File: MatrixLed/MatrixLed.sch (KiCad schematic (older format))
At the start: 68 parts

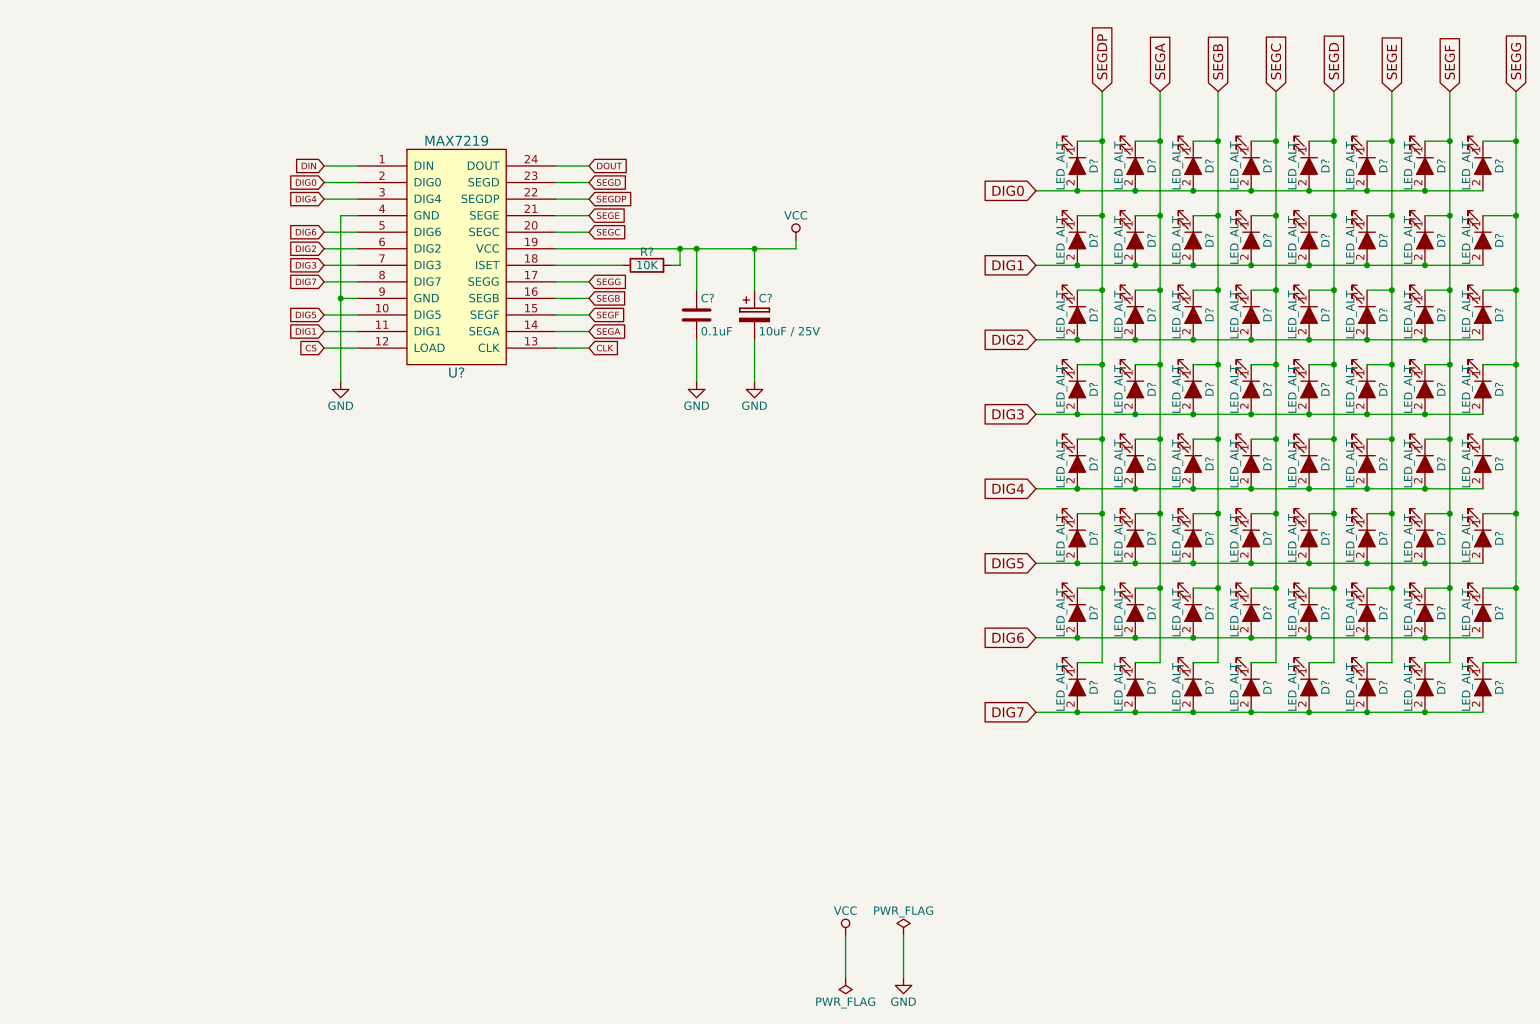
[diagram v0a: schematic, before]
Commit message: Leds girados para cambiar el MAX7219 por el HT16K33
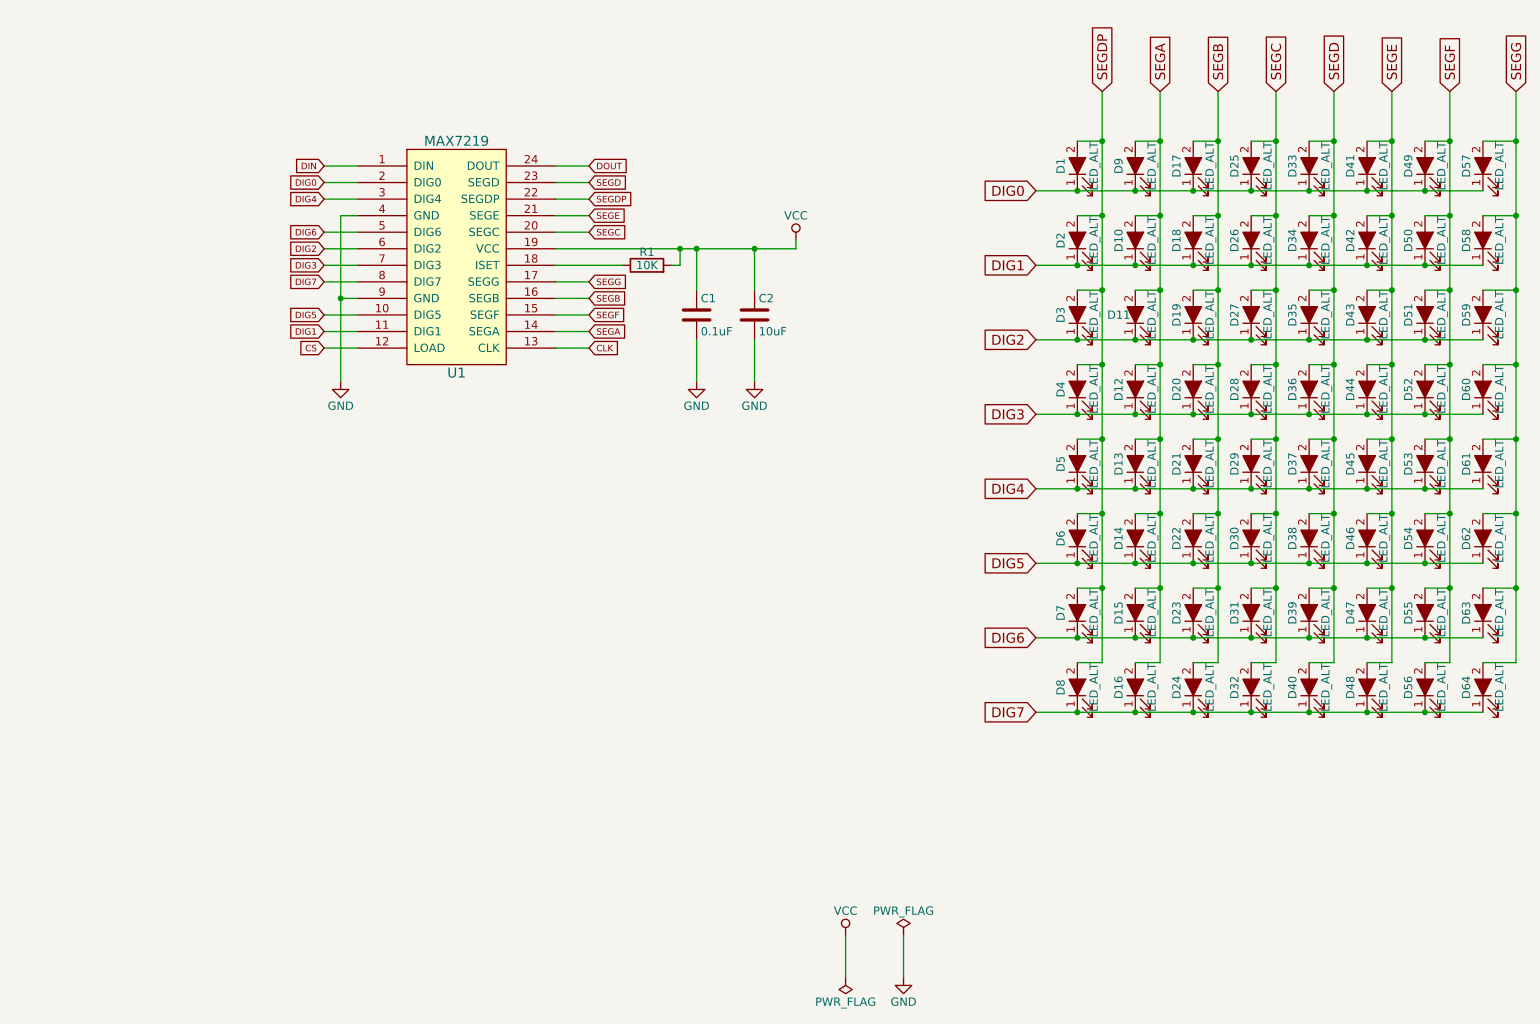
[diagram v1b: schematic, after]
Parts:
- removed C?: 10uF / 25V, symbol CP
- added C2: 10uF, symbol C
- gave numbers to parts that had none: 67
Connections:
- net DIG0: now also D1.1 (K), D17.1 (K), D25.1 (K), D33.1 (K), D41.1 (K), D49.1 (K), D57.1 (K), D9.1 (K); no longer D1.2 (A), D17.2 (A), D25.2 (A), D33.2 (A), D41.2 (A), D49.2 (A), D57.2 (A), D9.2 (A)
- net DIG1: now also D10.1 (K), D18.1 (K), D2.1 (K), D26.1 (K), D34.1 (K), D42.1 (K), D50.1 (K), D58.1 (K); no longer D10.2 (A), D18.2 (A), D2.2 (A), D26.2 (A), D34.2 (A), D42.2 (A), D50.2 (A), D58.2 (A)
- net DIG2: now also D11.1 (K), D19.1 (K), D27.1 (K), D3.1 (K), D35.1 (K), D43.1 (K), D51.1 (K), D59.1 (K); no longer D11.2 (A), D19.2 (A), D27.2 (A), D3.2 (A), D35.2 (A), D43.2 (A), D51.2 (A), D59.2 (A)
- net DIG3: now also D12.1 (K), D20.1 (K), D28.1 (K), D36.1 (K), D4.1 (K), D44.1 (K), D52.1 (K), D60.1 (K); no longer D12.2 (A), D20.2 (A), D28.2 (A), D36.2 (A), D4.2 (A), D44.2 (A), D52.2 (A), D60.2 (A)
- net DIG4: now also D13.1 (K), D21.1 (K), D29.1 (K), D37.1 (K), D45.1 (K), D5.1 (K), D53.1 (K), D61.1 (K); no longer D13.2 (A), D21.2 (A), D29.2 (A), D37.2 (A), D45.2 (A), D5.2 (A), D53.2 (A), D61.2 (A)
- net DIG5: now also D14.1 (K), D22.1 (K), D30.1 (K), D38.1 (K), D46.1 (K), D54.1 (K), D6.1 (K), D62.1 (K); no longer D14.2 (A), D22.2 (A), D30.2 (A), D38.2 (A), D46.2 (A), D54.2 (A), D6.2 (A), D62.2 (A)
- net DIG6: now also D15.1 (K), D23.1 (K), D31.1 (K), D39.1 (K), D47.1 (K), D55.1 (K), D63.1 (K), D7.1 (K); no longer D15.2 (A), D23.2 (A), D31.2 (A), D39.2 (A), D47.2 (A), D55.2 (A), D63.2 (A), D7.2 (A)
- net DIG7: now also D16.1 (K), D24.1 (K), D32.1 (K), D40.1 (K), D48.1 (K), D56.1 (K), D64.1 (K), D8.1 (K); no longer D16.2 (A), D24.2 (A), D32.2 (A), D40.2 (A), D48.2 (A), D56.2 (A), D64.2 (A), D8.2 (A)
- net GND: now also C2.2
- net SEGA: now also D10.2 (A), D11.2 (A), D12.2 (A), D13.2 (A), D14.2 (A), D15.2 (A), D16.2 (A), D9.2 (A); no longer D10.1 (K), D11.1 (K), D12.1 (K), D13.1 (K), D14.1 (K), D15.1 (K), D16.1 (K), D9.1 (K)
- net SEGB: now also D17.2 (A), D18.2 (A), D19.2 (A), D20.2 (A), D21.2 (A), D22.2 (A), D23.2 (A), D24.2 (A); no longer D17.1 (K), D18.1 (K), D19.1 (K), D20.1 (K), D21.1 (K), D22.1 (K), D23.1 (K), D24.1 (K)
- net SEGC: now also D25.2 (A), D26.2 (A), D27.2 (A), D28.2 (A), D29.2 (A), D30.2 (A), D31.2 (A), D32.2 (A); no longer D25.1 (K), D26.1 (K), D27.1 (K), D28.1 (K), D29.1 (K), D30.1 (K), D31.1 (K), D32.1 (K)
- net SEGD: now also D33.2 (A), D34.2 (A), D35.2 (A), D36.2 (A), D37.2 (A), D38.2 (A), D39.2 (A), D40.2 (A); no longer D33.1 (K), D34.1 (K), D35.1 (K), D36.1 (K), D37.1 (K), D38.1 (K), D39.1 (K), D40.1 (K)
- net SEGDP: now also D1.2 (A), D2.2 (A), D3.2 (A), D4.2 (A), D5.2 (A), D6.2 (A), D7.2 (A), D8.2 (A); no longer D1.1 (K), D2.1 (K), D3.1 (K), D4.1 (K), D5.1 (K), D6.1 (K), D7.1 (K), D8.1 (K)
- net SEGE: now also D41.2 (A), D42.2 (A), D43.2 (A), D44.2 (A), D45.2 (A), D46.2 (A), D47.2 (A), D48.2 (A); no longer D41.1 (K), D42.1 (K), D43.1 (K), D44.1 (K), D45.1 (K), D46.1 (K), D47.1 (K), D48.1 (K)
- net SEGF: now also D49.2 (A), D50.2 (A), D51.2 (A), D52.2 (A), D53.2 (A), D54.2 (A), D55.2 (A), D56.2 (A); no longer D49.1 (K), D50.1 (K), D51.1 (K), D52.1 (K), D53.1 (K), D54.1 (K), D55.1 (K), D56.1 (K)
- net SEGG: now also D57.2 (A), D58.2 (A), D59.2 (A), D60.2 (A), D61.2 (A), D62.2 (A), D63.2 (A), D64.2 (A); no longer D57.1 (K), D58.1 (K), D59.1 (K), D60.1 (K), D61.1 (K), D62.1 (K), D63.1 (K), D64.1 (K)
- net VCC: now also C2.1
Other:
- moved on the sheet: D1, D10, D11, D12, D13, D14, D15, D16, D17, D18, D19, D2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

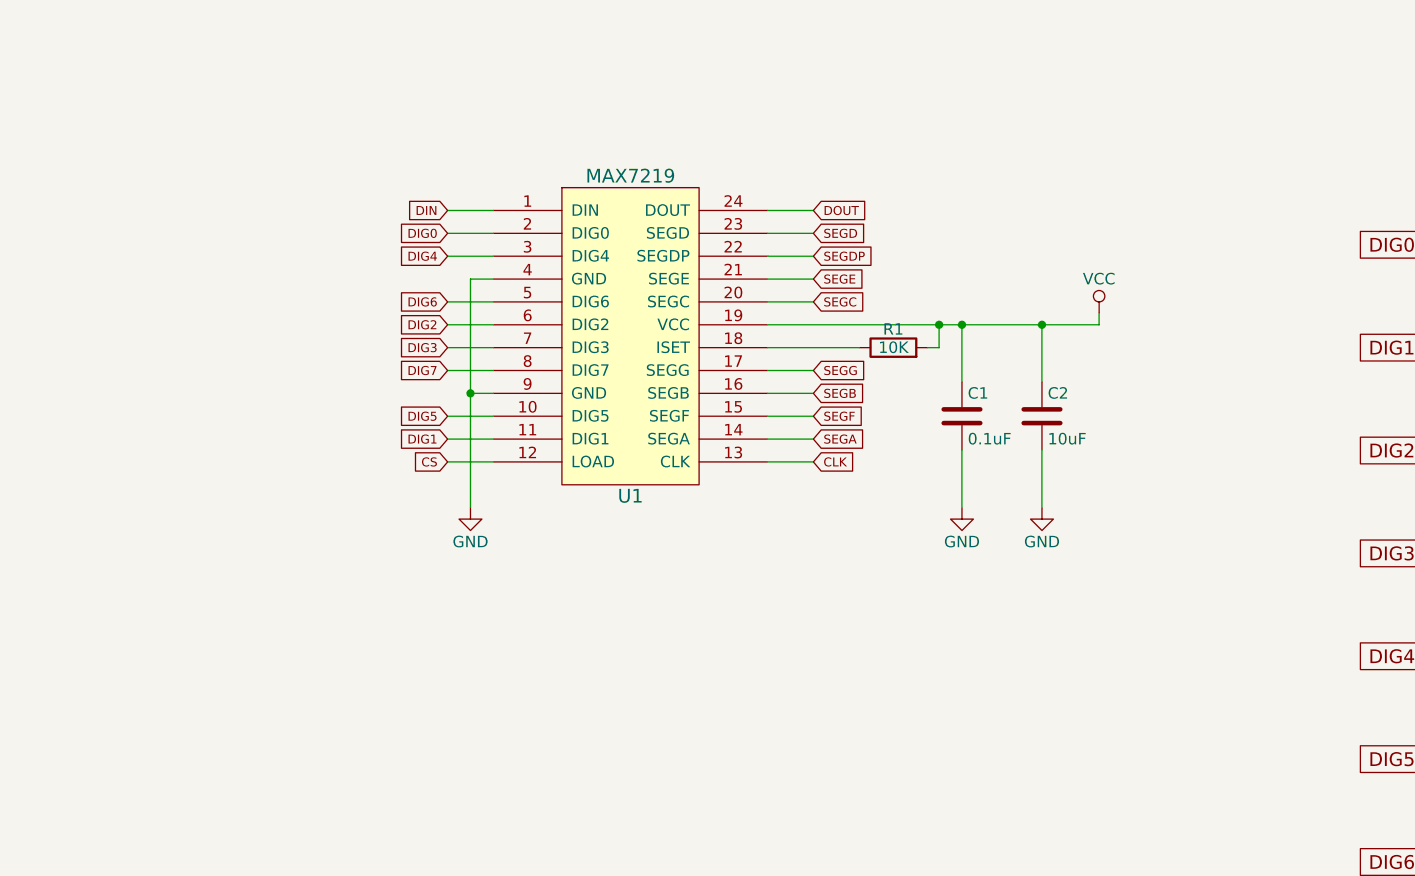
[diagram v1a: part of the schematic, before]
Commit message: Esquema terminado con el HT16K33, anotaciones hechas
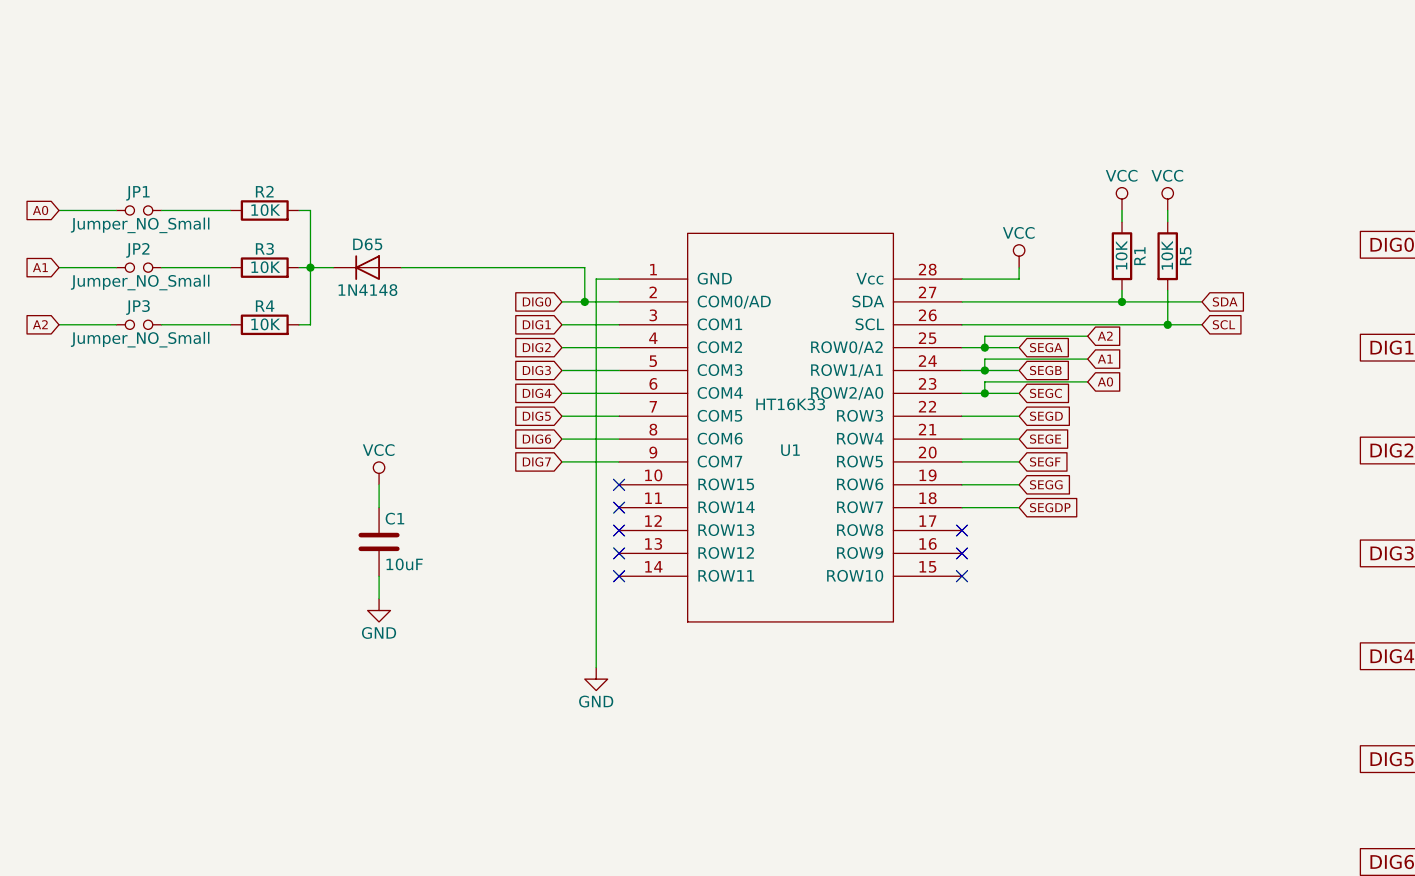
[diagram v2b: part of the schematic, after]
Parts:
- removed C2: 10uF, symbol C
- removed U1: MAX7219, symbol MAX7219
- added D65: 1N4148, Diodes_ThroughHole:D_DO-35_SOD27_Horizontal_RM10, symbol 1N4148
- added JP1, JP2, JP3: Jumper_NO_Small, symbol Jumper_NO_Small
- added R2, R3, R4, R5: 10K, symbol R
- added U1: HT16K33, MODULE, symbol HT16K33
- C1: value 0.1uF -> 10uF
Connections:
- net DIG0: now also D65.2 (A), U1.2 (COM0/AD)
- net DIG1: now also U1.3 (COM1)
- net DIG2: now also U1.4 (COM2)
- net DIG3: now also U1.5 (COM3)
- net DIG4: now also U1.6 (COM4)
- net DIG5: now also U1.7 (COM5)
- net DIG6: now also U1.8 (COM6)
- net DIG7: now also U1.9 (COM7)
- net GND: now also U1.1 (GND)
- net SEGD: now also U1.22 (ROW3)
- net SEGDP: now also U1.18 (ROW7)
- net SEGE: now also U1.21 (ROW4)
- net SEGF: now also U1.20 (ROW5)
- net SEGG: now also U1.19 (ROW6)
- net VCC: now also R1.1, R5.1, U1.28 (Vcc); no longer R1.2
- net SEGA renamed A2
- net A2: now also JP3.1, U1.25 (ROW0/A2)
- net SEGB renamed A1
- net A1: now also JP2.1, U1.24 (ROW1/A1)
- net SEGC renamed A0
- net A0: now also JP1.1, U1.23 (ROW2/A0)
- new net: JP1.2, R2.1
- new net: JP2.2, R3.1
- new net: JP3.2, R4.1
- new net: D65.1 (K), R2.2, R3.2, R4.2
- new net SCL: R5.2, U1.26 (SCL)
- new net SDA: R1.2, U1.27 (SDA)
- no-connect marks 0 -> 8
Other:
- moved on the sheet: R1

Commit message: DRC pasado y conector I2C añadido
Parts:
- added P1: CONN_01X04, symbol CONN_01X04
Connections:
- net GND: now also P1.1 (P1)
- net SCL: now also P1.3 (P3)
- net SDA: now also P1.4 (P4)
- net VCC: now also P1.2 (P2)
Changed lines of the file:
@@
 $EndComp
 $Comp
-L GND #PWR3
+L GND #PWR01
 U 1 1 58F84C6F
 P 3650 4450
-F 0 "#PWR3" H 3650 4200 50  0001 C CNN
+F 0 "#PWR01" H 3650 4200 50  0001 C CNN
 F 1 "GND" H 3650 4300 50  0000 C CNN
 F 2 "" H 3650 4450 50  0001 C CNN
@@
 $EndComp
 $Comp
-L VCC #PWR4
+L VCC #PWR02
 U 1 1 58F85EA5
 P 5500 2700
-F 0 "#PWR4" H 5500 2550 50  0001 C CNN
+F 0 "#PWR02" H 5500 2550 50  0001 C CNN
 F 1 "VCC" H 5500 2850 50  0000 C CNN
 F 2 "" H 5500 2700 50  0001 C CNN
@@
 $EndComp
 $Comp
-L PWR_FLAG #FLG2
-U 1 1 58F8D180
-P 6500 7100
-F 0 "#FLG2" H 6500 7175 50  0001 C CNN
-F 1 "PWR_FLAG" H 6500 7250 50  0000 C CNN
-F 2 "" H 6500 7100 50  0001 C CNN
-F 3 "" H 6500 7100 50  0001 C CNN
-	1    6500 7100
-	1    0    0    -1
-$EndComp
-$Comp
-L PWR_FLAG #FLG1
+L PWR_FLAG #FLG03
 U 1 1 58F8D47E
 P 6150 7350
-F 0 "#FLG1" H 6150 7425 50  0001 C CNN
+F 0 "#FLG03" H 6150 7425 50  0001 C CNN
 F 1 "PWR_FLAG" H 6150 7500 50  0000 C CNN
 F 2 "" H 6150 7350 50  0001 C CNN
@@
 $EndComp
 $Comp
-L GND #PWR8
-U 1 1 58F8DAA5
-P 6500 7350
-F 0 "#PWR8" H 6500 7100 50  0001 C CNN
-F 1 "GND" H 6500 7200 50  0000 C CNN
-F 2 "" H 6500 7350 50  0001 C CNN
-F 3 "" H 6500 7350 50  0001 C CNN
-	1    6500 7350
-	1    0    0    -1
-$EndComp
-$Comp
-L VCC #PWR7
+L VCC #PWR04
 U 1 1 58F8E72C
 P 6150 7100
-F 0 "#PWR7" H 6150 6950 50  0001 C CNN
+F 0 "#PWR04" H 6150 6950 50  0001 C CNN
 F 1 "VCC" H 6150 7250 50  0000 C CNN
 F 2 "" H 6150 7100 50  0001 C CNN
@@
 	6150 7100 6150 7350
 Wire Wire Line
-	6500 7350 6500 7100
-Wire Wire Line
 	3750 2850 3500 2850
 Wire Wire Line
@@
 Connection ~ 6150 2950
 $Comp
-L VCC #PWR5
+L VCC #PWR05
 U 1 1 58F52AD8
 P 5950 2450
-F 0 "#PWR5" H 5950 2300 50  0001 C CNN
+F 0 "#PWR05" H 5950 2300 50  0001 C CNN
 F 1 "VCC" H 5950 2600 50  0000 C CNN
 F 2 "" H 5950 2450 50  0001 C CNN
@@
 $EndComp
 $Comp
-L VCC #PWR6
+L VCC #PWR06
 U 1 1 58F52BAC
 P 6150 2450
-F 0 "#PWR6" H 6150 2300 50  0001 C CNN
+F 0 "#PWR06" H 6150 2300 50  0001 C CNN
 F 1 "VCC" H 6150 2600 50  0000 C CNN
 F 2 "" H 6150 2450 50  0001 C CNN
@@
 $EndComp
 $Comp
-L GND #PWR2
+L GND #PWR07
 U 1 1 58F581AE
 P 2700 4150
-F 0 "#PWR2" H 2700 3900 50  0001 C CNN
+F 0 "#PWR07" H 2700 3900 50  0001 C CNN
 F 1 "GND" H 2700 4000 50  0000 C CNN
 F 2 "" H 2700 4150 50  0001 C CNN
@@
 $EndComp
 $Comp
-L VCC #PWR1
+L VCC #PWR08
 U 1 1 58F58411
 P 2700 3650
-F 0 "#PWR1" H 2700 3500 50  0001 C CNN
+F 0 "#PWR08" H 2700 3500 50  0001 C CNN
 F 1 "VCC" H 2700 3800 50  0000 C CNN
 F 2 "" H 2700 3650 50  0001 C CNN
@@
 Wire Wire Line
 	2700 4050 2700 4150
+$Comp
+L CONN_01X04 P1
+U 1 1 58F5A430
+P 3050 5150
+F 0 "P1" H 3050 5400 50  0000 C CNN
+F 1 "CONN_01X04" V 3150 5150 50  0000 C CNN
+F 2 "" H 3050 5150 50  0001 C CNN
+F 3 "" H 3050 5150 50  0001 C CNN
+	1    3050 5150
+	-1   0    0    1
+$EndComp
+$Comp
+L GND #PWR09
+U 1 1 58F5AB17
+P 3350 5350
+F 0 "#PWR09" H 3350 5100 50  0001 C CNN
+F 1 "GND" H 3350 5200 50  0000 C CNN
+F 2 "" H 3350 5350 50  0001 C CNN
+F 3 "" H 3350 5350 50  0001 C CNN
+	1    3350 5350
+	1    0    0    -1
+$EndComp
+Wire Wire Line
+	3250 5300 3350 5300
+Wire Wire Line
+	3350 5300 3350 5350
+Wire Wire Line
+	3250 5000 3600 5000
+Wire Wire Line
+	3250 5100 3600 5100
+Wire Wire Line
+	3250 5200 3350 5200
+Wire Wire Line
+	3350 5200 3350 4900
+$Comp
+L VCC #PWR010
+U 1 1 58F5B504
+P 3350 4900
+F 0 "#PWR010" H 3350 4750 50  0001 C CNN
+F 1 "VCC" H 3350 5050 50  0000 C CNN
+F 2 "" H 3350 4900 50  0001 C CNN
+F 3 "" H 3350 4900 50  0001 C CNN
+	1    3350 4900
+	1    0    0    -1
+$EndComp
+Text GLabel 3600 5000 2    39   Input ~ 0
+SDA
+Text GLabel 3600 5100 2    39   Input ~ 0
+SCL
 $EndSCHEMATC
